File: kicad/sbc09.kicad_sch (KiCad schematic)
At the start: 77 parts, among them J1 Conn_01x03_Male, J2 Conn_01x06_Male, J3 Conn_01x06_Male, J4 Conn_01x06_Male, J5 DB9_Female_MountingHoles, J6 Conn_02x25_Odd_Even, Q1 2N7000, SW1 SW_Push, U1 74LS245, U10 74LS670, U11 74LS670, U12 AS6C4008-55PCN, U13 SST39SF040-DIP, U14 SST39SF040-DIP, U15 XR68C681CJ, U16 MAX232, U2 74LS245, U3 74LS245, U4 MC6809E, U5 74HCT125, U6 ATF22V10C, U7 ATF22V10C, U8 74LS670, U9 74LS670, X1 8MHz, X2 3.6864MHz

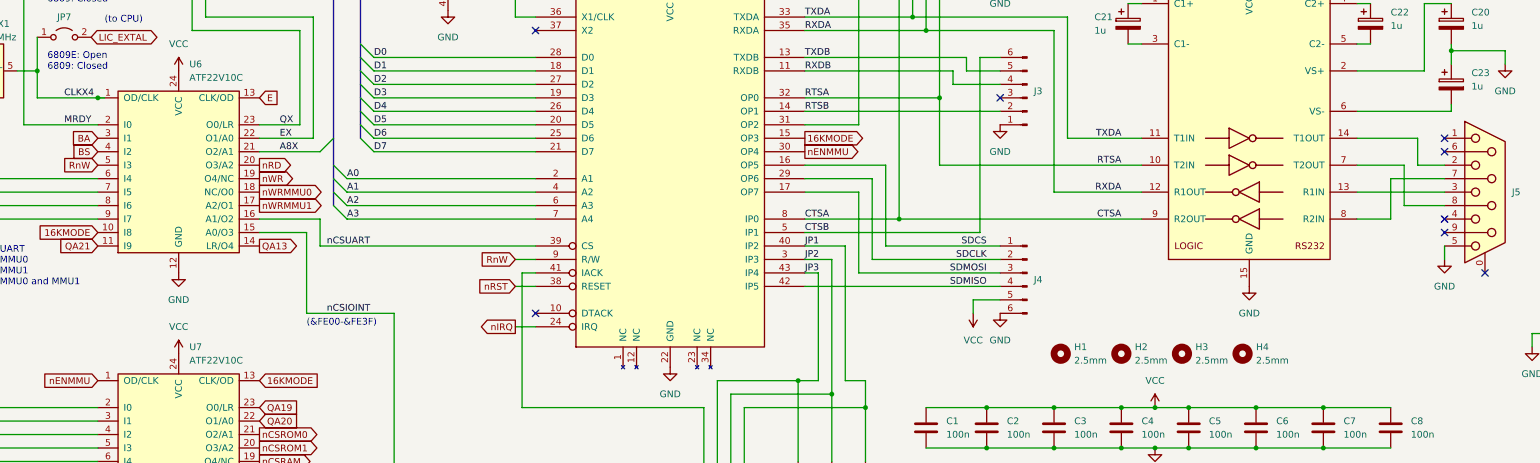
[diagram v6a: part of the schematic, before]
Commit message: Name serial port nets
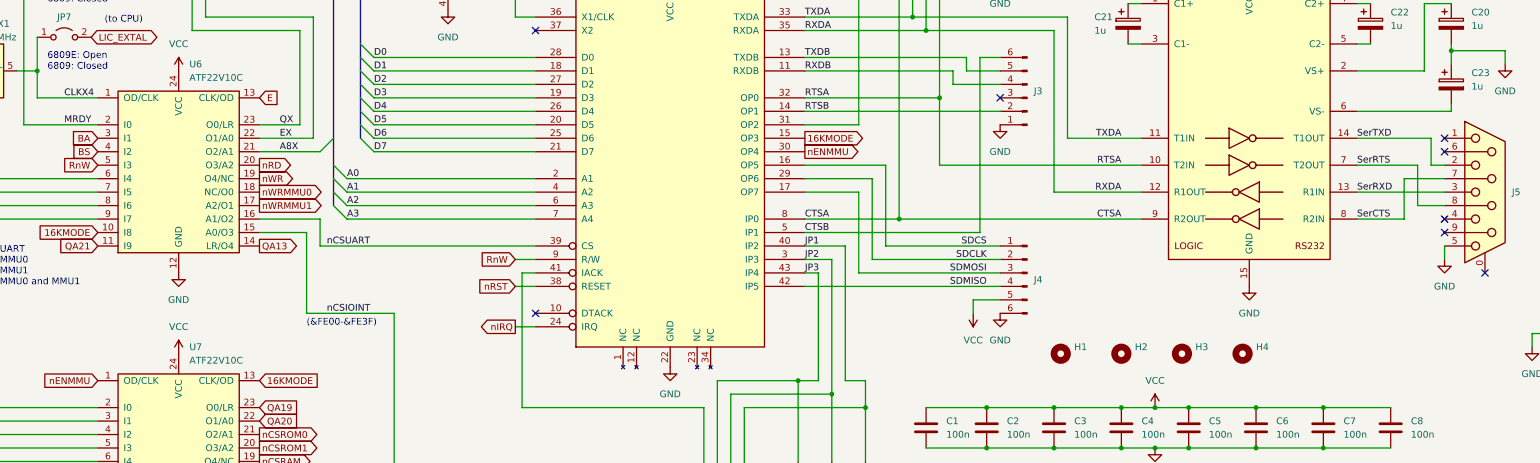
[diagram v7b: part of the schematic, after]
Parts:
- H1, H2, H3, H4: value 2.5mm -> (none)
- J4: footprint (none) -> Connector_PinSocket_2.54mm:PinSocket_1x06_P2.54mm_Horizontal
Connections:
- net SerTXD: now reaches J5.2, U16.14 (T1OUT)
- net SerRXD: now reaches J5.3, U16.13 (R1IN)
- net SerCTS: now reaches J5.7, U16.8 (R2IN)
- net SerRTS: now reaches J5.8, U16.7 (T2OUT)
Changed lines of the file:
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@@
   (junction (at 214.63 278.13) (diameter 0) (color 0 0 0 0)
   )
-  (junction (at 46.99 190.5) (diameter 0) (color 0 0 0 0)
-  )
   (junction (at 374.65 224.79) (diameter 0) (color 0 0 0 0)
   )
@@
     (stroke (width 0) (type default) (color 0 0 0 0))
   )
-  (wire (pts (xy 295.91 203.2) (xy 295.91 198.12))
+  (wire (pts (xy 298.45 203.2) (xy 298.45 198.12))
     (stroke (width 0) (type default) (color 0 0 0 0))
   )
@@
     (stroke (width 0) (type default) (color 0 0 0 0))
   )
-  (wire (pts (xy 290.83 213.36) (xy 284.48 213.36))
+  (wire (pts (xy 293.37 213.36) (xy 284.48 213.36))
     (stroke (width 0) (type default) (color 0 0 0 0))
   )
@@
     (stroke (width 0) (type default) (color 0 0 0 0))
   )
-  (wire (pts (xy 300.99 205.74) (xy 290.83 205.74))
+  (wire (pts (xy 300.99 205.74) (xy 293.37 205.74))
     (stroke (width 0) (type default) (color 0 0 0 0))
   )
@@
     (stroke (width 0) (type default) (color 0 0 0 0))
   )
-  (wire (pts (xy 295.91 198.12) (xy 284.48 198.12))
+  (wire (pts (xy 298.45 198.12) (xy 284.48 198.12))
     (stroke (width 0) (type default) (color 0 0 0 0))
   )
@@
     (stroke (width 0) (type default) (color 0 0 0 0))
   )
-  (wire (pts (xy 293.37 203.2) (xy 284.48 203.2))
+  (wire (pts (xy 295.91 203.2) (xy 284.48 203.2))
     (stroke (width 0) (type default) (color 0 0 0 0))
   )
@@
     (stroke (width 0) (type default) (color 0 0 0 0))
   )
-  (wire (pts (xy 46.99 190.5) (xy 48.26 190.5))
-    (stroke (width 0) (type default) (color 0 0 0 0))
-  )
   (wire (pts (xy 88.9 88.9) (xy 88.9 99.06))
     (stroke (width 0) (type default) (color 0 0 0 0))
@@
     (stroke (width 0) (type default) (color 0 0 0 0))
   )
-  (wire (pts (xy 290.83 205.74) (xy 290.83 213.36))
+  (wire (pts (xy 293.37 205.74) (xy 293.37 213.36))
     (stroke (width 0) (type default) (color 0 0 0 0))
   )
@@
     (stroke (width 0) (type default) (color 0 0 0 0))
   )
-  (wire (pts (xy 300.99 210.82) (xy 293.37 210.82))
+  (wire (pts (xy 300.99 210.82) (xy 295.91 210.82))
     (stroke (width 0) (type default) (color 0 0 0 0))
   )
@@
     (stroke (width 0) (type default) (color 0 0 0 0))
   )
-  (wire (pts (xy 300.99 203.2) (xy 295.91 203.2))
+  (wire (pts (xy 300.99 203.2) (xy 298.45 203.2))
     (stroke (width 0) (type default) (color 0 0 0 0))
   )
@@
     (stroke (width 0) (type default) (color 0 0 0 0))
   )
-  (wire (pts (xy 293.37 210.82) (xy 293.37 203.2))
+  (wire (pts (xy 295.91 210.82) (xy 295.91 203.2))
     (stroke (width 0) (type default) (color 0 0 0 0))
   )
@@
     (effects (font (size 1.27 1.27)) (justify left bottom))
   )
+  (label "SerRTS" (at 284.48 203.2 0)
+    (effects (font (size 1.27 1.27)) (justify left bottom))
+  )
   (label "A9" (at 365.76 93.98 0)
     (effects (font (size 1.27 1.27)) (justify left bottom))
@@
     (effects (font (size 1.27 1.27)) (justify left bottom))
   )
+  (label "SerTXD" (at 284.48 198.12 0)
+    (effects (font (size 1.27 1.27)) (justify left bottom))
+  )
   (label "A1" (at 99.06 115.57 0)
     (effects (font (size 1.27 1.27)) (justify left bottom))
@@
     (effects (font (size 1.27 1.27)) (justify left bottom))
   )
+  (label "SerCTS" (at 284.48 213.36 0)
+    (effects (font (size 1.27 1.27)) (justify left bottom))
+  )
   (label "A15" (at 158.75 66.04 0)
     (effects (font (size 1.27 1.27)) (justify left bottom))
@@
     (effects (font (size 1.27 1.27)) (justify left bottom))
   )
+  (label "SerRXD" (at 284.48 208.28 0)
+    (effects (font (size 1.27 1.27)) (justify left bottom))
+  )
   (global_label "Q" (shape input) (at 326.39 241.3 180) (fields_autoplaced)
     (effects (font (size 1.27 1.27)) (justify right))
@@
       (effects (font (size 1.27 1.27)) (justify left))
     )
-    (property "Value" "2.5mm" (id 1) (at 231.14 240.0299 0)
+    (property "Value" "" (id 1) (at 231.14 240.0299 0)
       (effects (font (size 1.27 1.27)) (justify left))
     )
@@
       (effects (font (size 1.27 1.27)) (justify left))
     )
-    (property "Value" "2.5mm" (id 1) (at 242.57 240.0299 0)
+    (property "Value" "" (id 1) (at 242.57 240.0299 0)
       (effects (font (size 1.27 1.27)) (justify left))
     )
@@
       (effects (font (size 1.27 1.27)) (justify left))
     )
-    (property "Value" "2.5mm" (id 1) (at 254 240.0299 0)
+    (property "Value" "" (id 1) (at 254 240.0299 0)
       (effects (font (size 1.27 1.27)) (justify left))
     )
@@
       (effects (font (size 1.27 1.27)) (justify right) hide)
     )
-    (property "Footprint" "" (id 2) (at 222.25 223.52 0)
+    (property "Footprint" "Connector_PinSocket_2.54mm:PinSocket_1x06_P2.54mm_Horizontal" (id 2) (at 222.25 223.52 0)
       (effects (font (size 1.27 1.27)) hide)
     )
@@
       (effects (font (size 1.27 1.27)) (justify left))
     )
-    (property "Value" "2.5mm" (id 1) (at 265.43 240.0299 0)
+    (property "Value" "" (id 1) (at 265.43 240.0299 0)
       (effects (font (size 1.27 1.27)) (justify left))
     )
@@
     )
     (path "/0fdc7ebb-4b15-4947-a92f-73b17a1787e1"
-      (reference "H1") (unit 1) (value "2.5mm") (footprint "MountingHole:MountingHole_2.7mm")
+      (reference "H1") (unit 1) (value "2.7mm") (footprint "MountingHole:MountingHole_2.7mm")
     )
     (path "/5674ce8a-3392-4411-803e-631fd34945b3"
-      (reference "H2") (unit 1) (value "2.5mm") (footprint "MountingHole:MountingHole_2.7mm")
+      (reference "H2") (unit 1) (value "2.7mm") (footprint "MountingHole:MountingHole_2.7mm")
     )
     (path "/6454d29e-e337-4421-a0c1-bd1704ff0e10"
-      (reference "H3") (unit 1) (value "2.5mm") (footprint "MountingHole:MountingHole_2.7mm")
+      (reference "H3") (unit 1) (value "2.7mm") (footprint "MountingHole:MountingHole_2.7mm")
     )
     (path "/aec67b2c-17ba-4429-80e9-89cc778d77b9"
-      (reference "H4") (unit 1) (value "2.5mm") (footprint "MountingHole:MountingHole_2.7mm")
+      (reference "H4") (unit 1) (value "2.7mm") (footprint "MountingHole:MountingHole_2.7mm")
     )
     (path "/2d3bef94-9857-4263-bb09-146a0d34f7ef"
